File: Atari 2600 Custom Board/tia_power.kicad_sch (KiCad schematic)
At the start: 0 parts

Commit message: Added main ICs to schematic
Added main ICs to schematic
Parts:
- added U4: ~, symbol Atari2600_Library:TIA-NTSC
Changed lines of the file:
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@@
 	(generator_version "8.0")
 	(paper "A4")
+	(symbol
+		(lib_id "Atari2600_Library:TIA-NTSC")
+		(at 111.76 43.18 0)
+		(unit 1)
+		(exclude_from_sim no)
+		(in_bom yes)
+		(on_board yes)
+		(dnp no)
+		(fields_autoplaced yes)
+		(property "Reference" "U4"
+			(at 123.19 39.37 0)
+			(effects
+				(font
+					(size 1.27 1.27)
+				)
+			)
+		)
+		(property "Value" "~"
+			(at 123.19 41.91 0)
+			(effects
+				(font
+					(size 1.27 1.27)
+				)
+			)
+		)
+		(property "Footprint" ""
+			(at 111.76 43.18 0)
+			(effects
+				(font
+					(size 1.27 1.27)
+				)
+				(hide yes)
+			)
+		)
+		(property "Datasheet" ""
+			(at 111.76 43.18 0)
+			(effects
+				(font
+					(size 1.27 1.27)
+				)
+				(hide yes)
+			)
+		)
+		(property "Description" ""
+			(at 111.76 43.18 0)
+			(effects
+				(font
+					(size 1.27 1.27)
+				)
+				(hide yes)
+			)
+		)
+		(pin "17"
+		)
+		(pin "24"
+		)
+		(pin "32"
+		)
+		(pin "36"
+		)
+		(pin "23"
+		)
+		(pin "16"
+		)
+		(pin "28"
+		)
+		(pin "3"
+		)
+		(pin "19"
+		)
+		(pin "30"
+		)
+		(pin "38"
+		)
+		(pin "4"
+		)
+		(pin "40"
+		)
+		(pin "11"
+		)
+		(pin "34"
+		)
+		(pin "9"
+		)
+		(pin "26"
+		)
+		(pin "14"
+		)
+		(pin "21"
+		)
+		(pin "31"
+		)
+		(pin "10"
+		)
+		(pin "20"
+		)
+		(pin "18"
+		)
+		(pin "22"
+		)
+		(pin "35"
+		)
+		(pin "37"
+		)
+		(pin "5"
+		)
+		(pin "6"
+		)
+		(pin "2"
+		)
+		(pin "15"
+		)
+		(pin "13"
+		)
+		(pin "8"
+		)
+		(pin "29"
+		)
+		(pin "39"
+		)
+		(pin "25"
+		)
+		(pin "27"
+		)
+		(pin "33"
+		)
+		(pin "7"
+		)
+		(pin "1"
+		)
+		(pin "12"
+		)
+		(instances
+			(project "atari2600"
+				(path "/d26a1e82-f8cb-48a3-8cce-edbb66ba228a/1512de0d-3d07-49f3-86b5-e084744fd125"
+					(reference "U4")
+					(unit 1)
+				)
+			)
+		)
+	)
 )

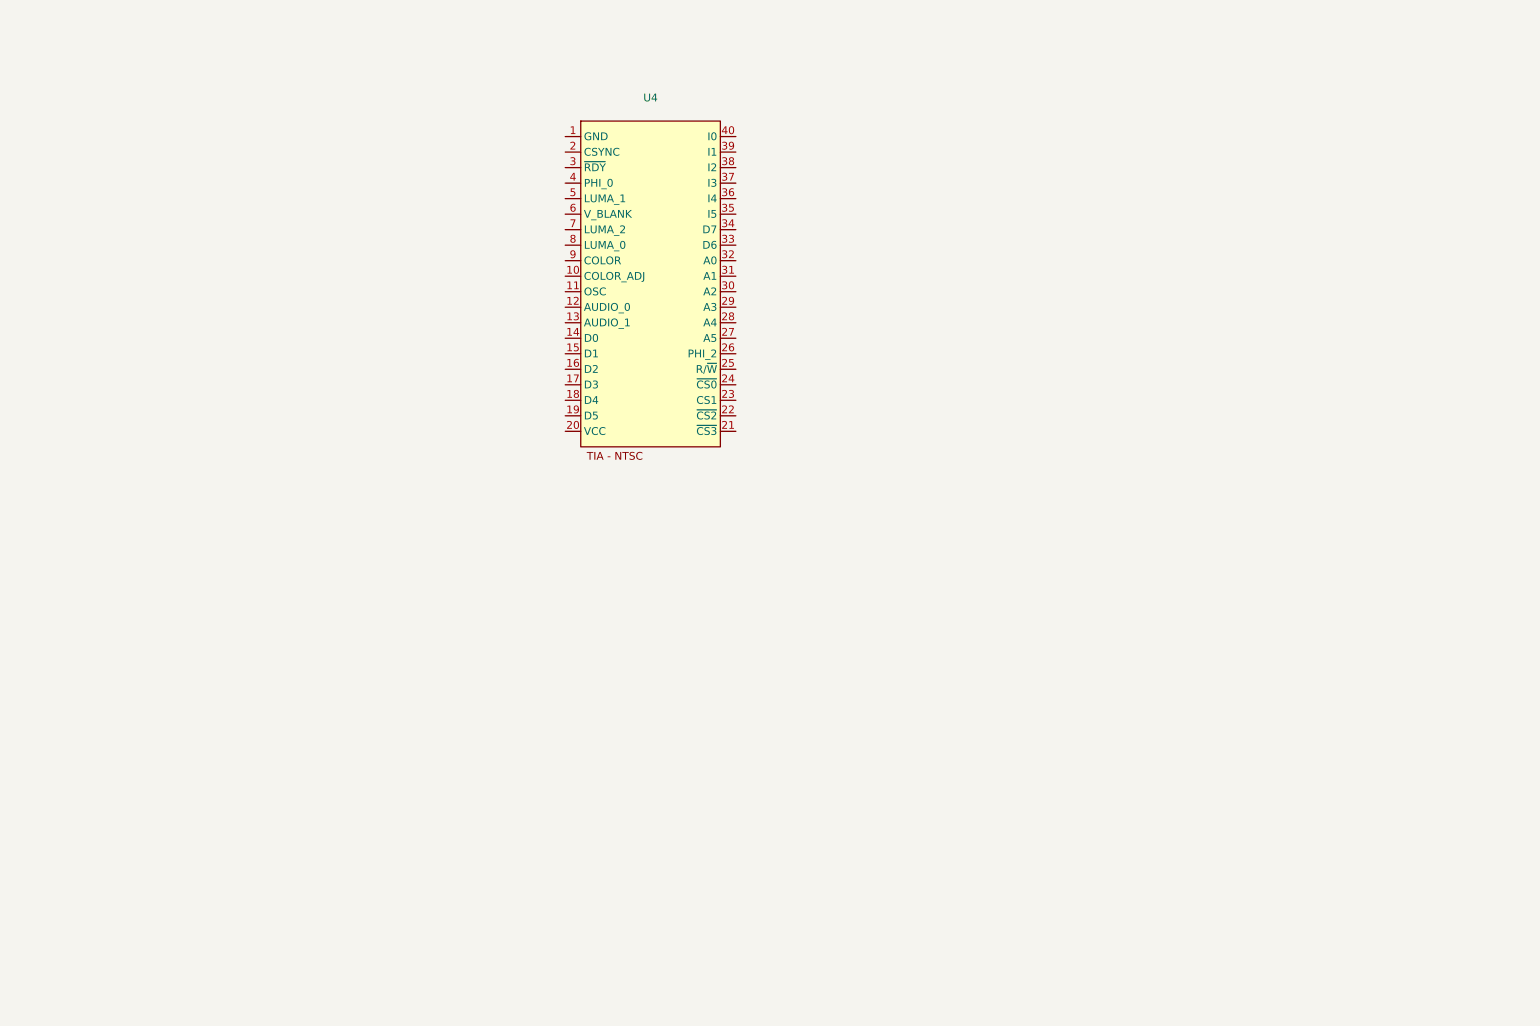
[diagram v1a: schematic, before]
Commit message: Update tia_power.kicad_sch
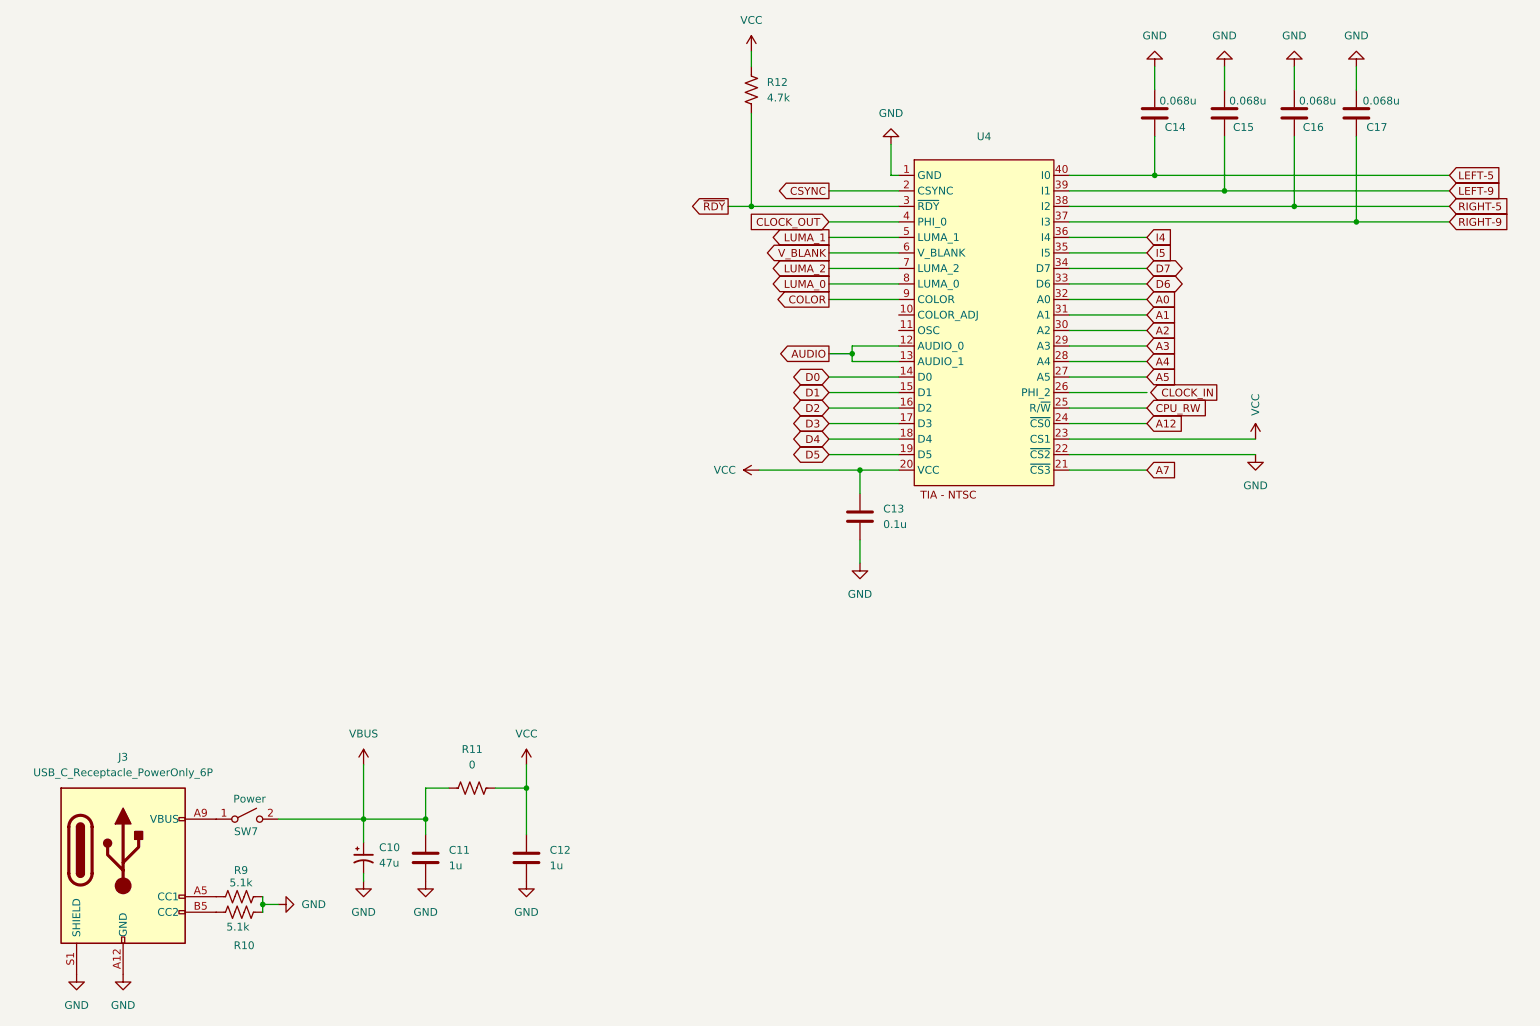
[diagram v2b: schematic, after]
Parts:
- added C10: 47u, symbol Device:C_Polarized_Small_US
- added C11, C12: 1u, symbol Device:C
- added C13: 0.1u, symbol Device:C
- added C14, C15, C16, C17: 0.068u, symbol Device:C
- added J3: USB_C_Receptacle_PowerOnly_6P, symbol Connector:USB_C_Receptacle_PowerOnly_6P
- added R10, R9: 5.1k, symbol Device:R_US
- added R11: 0, symbol Device:R_US
- added R12: 4.7k, symbol Device:R_US
- added SW7: Power, symbol Switch:SW_SPST
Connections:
- net GND: now reaches U4.1 (GND)
- net GND: now also U4.22 (~{CS2}), C10.2, C11.2, C12.2, C13.2, C14.2, C15.2, C16.2, C17.2, J3.A12 (GND), J3.B12 (GND), J3.S1 (SHIELD), R10.1, R9.2
- net AUDIO: now reaches U4.12 (AUDIO_0)
- net AUDIO: now also U4.13 (AUDIO_1)
- net D0: now reaches U4.14 (D0)
- net D1: now reaches U4.15 (D1)
- net D2: now reaches U4.16 (D2)
- net D3: now reaches U4.17 (D3)
- net D4: now reaches U4.18 (D4)
- net D5: now reaches U4.19 (D5)
- net CSYNC: now reaches U4.2 (CSYNC)
- net VCC: now reaches U4.20 (VCC)
- net VCC: now also U4.23 (CS1), C12.1, C13.1, R11.2, R12.1
- net A7: now reaches U4.21 (~{CS3})
- net A12: now reaches U4.24 (~{CS0})
- net CPU_RW: now reaches U4.25 (R/~{W})
- net A5: now reaches U4.27 (A5)
- net A4: now reaches U4.28 (A4)
- net A3: now reaches U4.29 (A3)
- net ~{RDY}: now reaches U4.3 (~{RDY})
- net ~{RDY}: now also R12.2
- net A2: now reaches U4.30 (A2)
- net A1: now reaches U4.31 (A1)
- net A0: now reaches U4.32 (A0)
- net D6: now reaches U4.33 (D6)
- net D7: now reaches U4.34 (D7)
- net I5: now reaches U4.35 (I5)
- net I4: now reaches U4.36 (I4)
- net RIGHT-9: now reaches U4.37 (I3)
- net RIGHT-9: now also C17.1
- net RIGHT-5: now reaches U4.38 (I2)
- net RIGHT-5: now also C16.1
- net LEFT-9: now reaches U4.39 (I1)
- net LEFT-9: now also C15.1
- net CLOCK_OUT: now reaches U4.4 (PHI_0)
- net LEFT-5: now reaches U4.40 (I0)
- net LEFT-5: now also C14.1
- net LUMA_1: now reaches U4.5 (LUMA_1)
- net V_BLANK: now reaches U4.6 (V_BLANK)
- net LUMA_2: now reaches U4.7 (LUMA_2)
- net LUMA_0: now reaches U4.8 (LUMA_0)
- net COLOR: now reaches U4.9 (COLOR)
- new net: J3.A5 (CC1), R9.1
- new net: J3.B5 (CC2), R10.2
- new net: J3.A9 (VBUS), J3.B9 (VBUS), SW7.1 (A)
- new net VBUS: C10.1, C11.1, R11.1, SW7.2 (B)
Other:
- moved on the sheet: U4

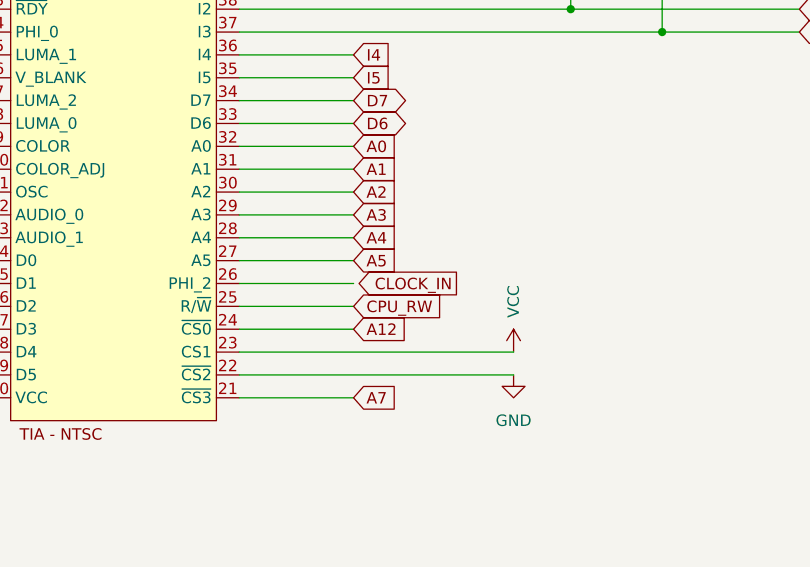
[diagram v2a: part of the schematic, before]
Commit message: Update tia_power.kicad_sch
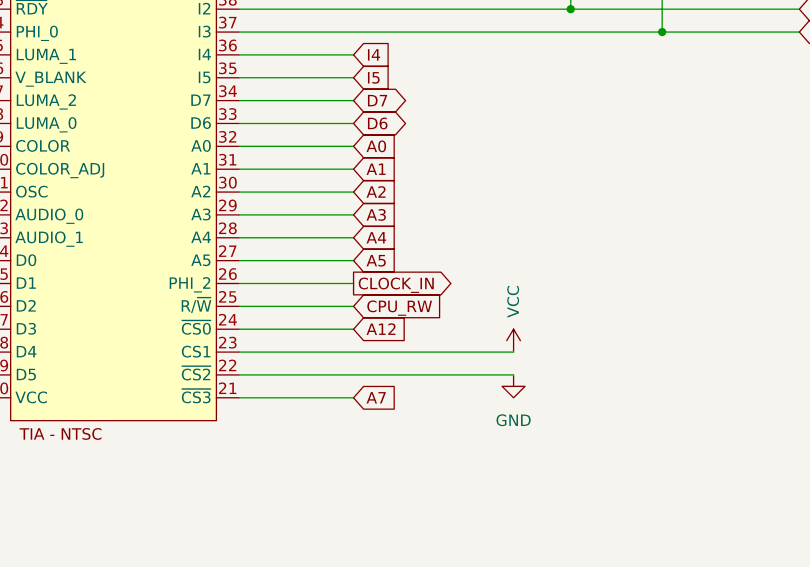
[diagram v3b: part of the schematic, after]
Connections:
- net CLOCK_IN: now also U4.26 (PHI_2)
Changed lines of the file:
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@@
 	(global_label "CLOCK_IN"
 		(shape output)
-		(at 215.9 87.63 180)
+		(at 204.47 87.63 0)
 		(fields_autoplaced yes)
 		(effects
@@
 				(size 1.27 1.27)
 			)
-			(justify right)
+			(justify left)
 		)
 		(property "Intersheetrefs" "${INTERSHEET_REFS}"
-			(at 203.8433 87.63 0)
+			(at 216.5267 87.63 0)
 			(effects
 				(font
 					(size 1.27 1.27)
 				)
-				(justify right)
+				(justify left)
 				(hide yes)
 			)

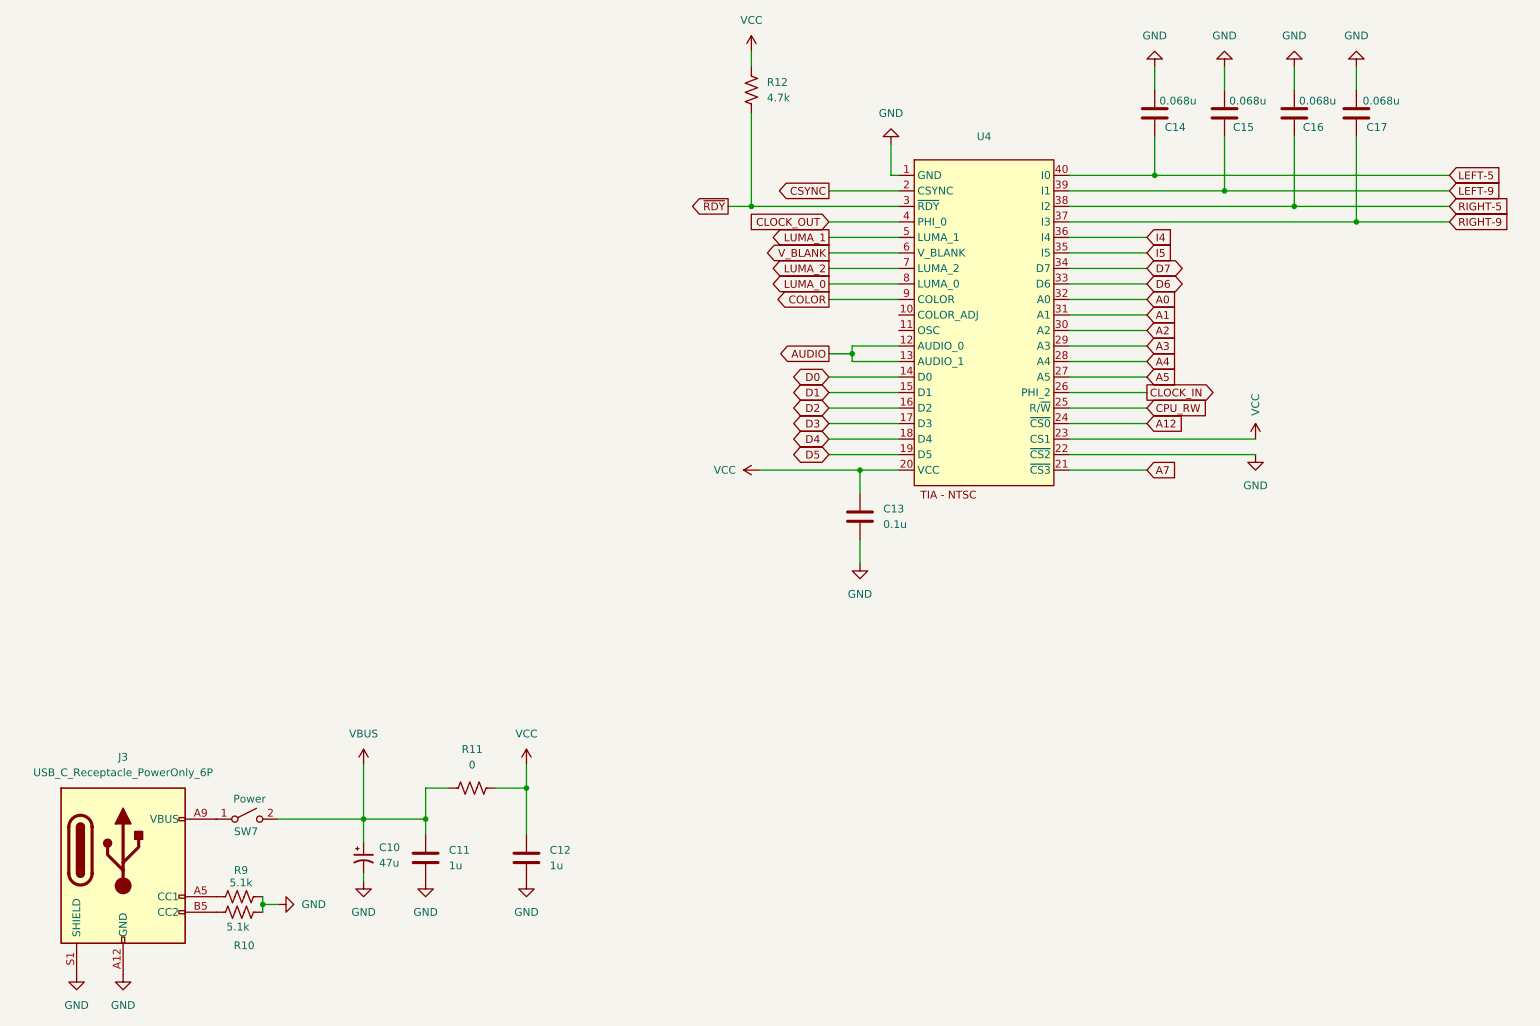
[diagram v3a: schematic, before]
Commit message: Update tia_power.kicad_sch
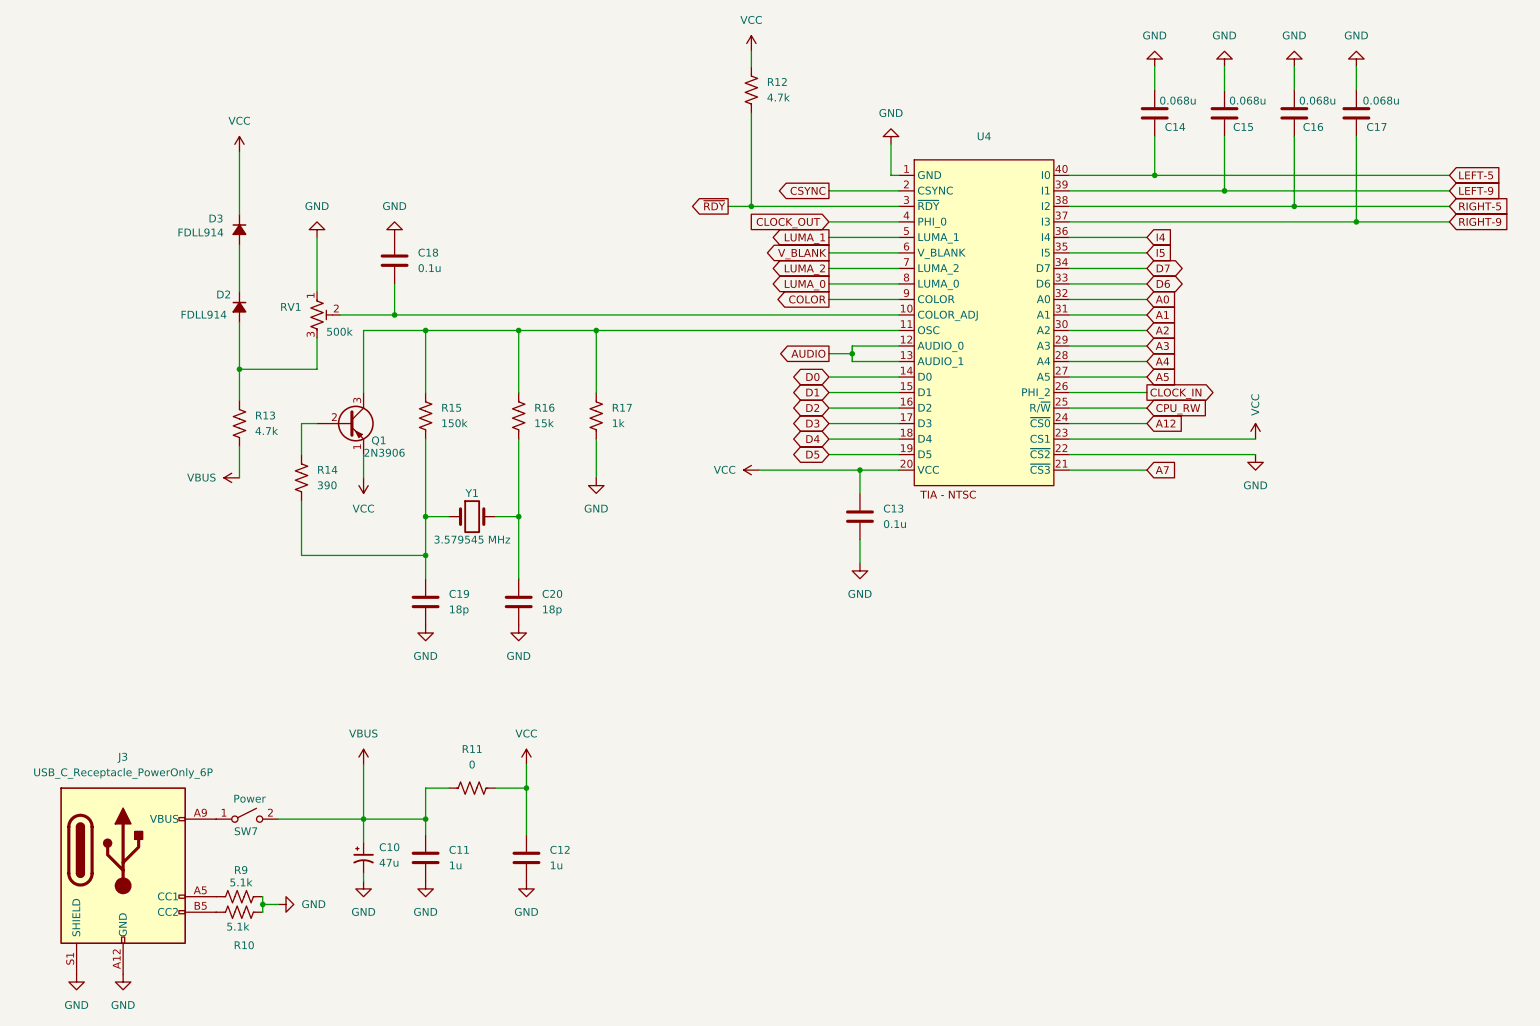
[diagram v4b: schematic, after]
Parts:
- added C18: 0.1u, symbol Device:C
- added C19, C20: 18p, symbol Device:C
- added D2, D3: FDLL914, symbol Device:D_Small_Filled
- added Q1: 2N3906, Package_TO_SOT_THT:TO-92_Inline, symbol Transistor_BJT:2N3906
- added R13: 4.7k, symbol Device:R_US
- added R14: 390, symbol Device:R_US
- added R15: 150k, symbol Device:R_US
- added R16: 15k, symbol Device:R_US
- added R17: 1k, symbol Device:R_US
- added RV1: 500k, symbol Device:R_Potentiometer_Trim_US
- added Y1: 3.579545 MHz, symbol Device:Crystal
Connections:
- net GND: now also C18.1, C19.2, C20.2, R17.1, RV1.1
- net VBUS: now also R13.1
- net VCC: now also D3.1 (K), Q1.1 (E)
- net at U4.10 (COLOR_ADJ): now also C18.2, RV1.2
- net at U4.11 (OSC): now also Q1.3 (C), R15.2, R16.2, R17.2
- new net: D2.2 (A), R13.2, RV1.3
- new net: D2.1 (K), D3.2 (A)
- new net: C19.1, R14.1, R15.1, Y1.1
- new net: Q1.2 (B), R14.2
- new net: C20.1, R16.1, Y1.2
